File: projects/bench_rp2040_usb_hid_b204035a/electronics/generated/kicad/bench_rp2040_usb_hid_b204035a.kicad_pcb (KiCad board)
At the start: 2 copper layers, 51 x 21 mm, 14 parts, among them J1 USB-C POWER, J2 SWD 10-pin, U1 3V3 LDO, U2 RP2040, U3 2MB QSPI, X1 12MHz XTAL

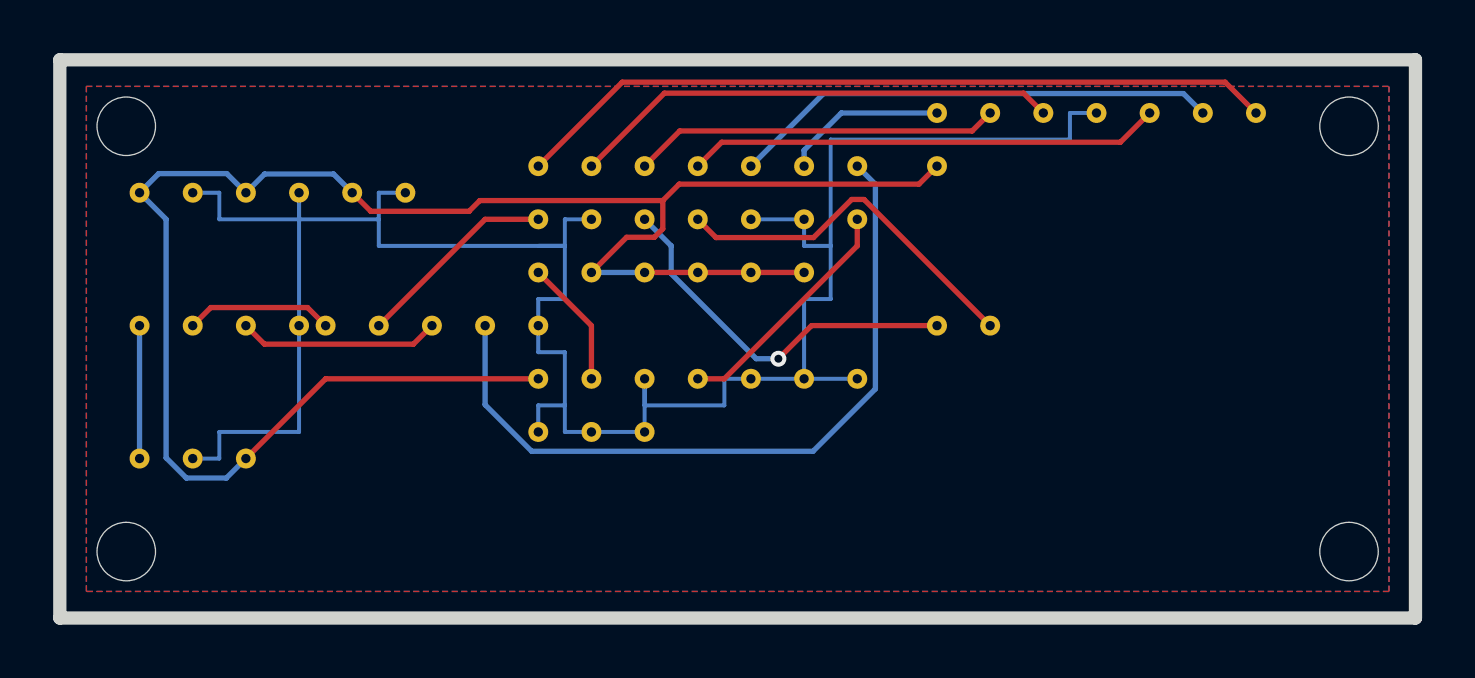
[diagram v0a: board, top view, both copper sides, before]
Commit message: fix: ground rp2040 power path evidence
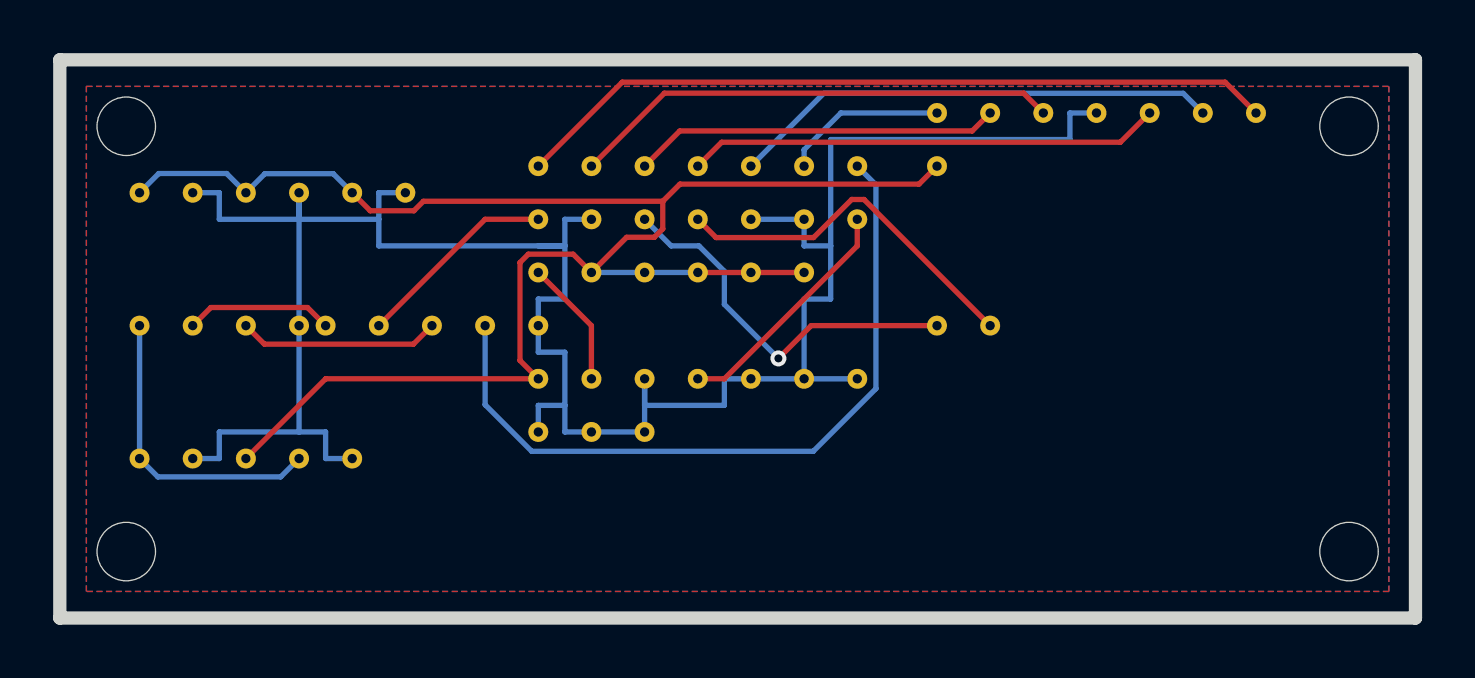
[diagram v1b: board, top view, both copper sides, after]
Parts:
- added C4: 10uF USB_IN, Capacitor_SMD:C_0603_1608Metric, F.Cu at (9.00, 15.0)
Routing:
- net USB_VBUS: track 5.00 -> 11.6 mm
- net V3V3: track 70.8 -> 64.6 mm
- net GND: track 88.0 -> 91.0 mm
